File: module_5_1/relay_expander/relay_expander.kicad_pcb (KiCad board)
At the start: 2 copper layers, 1 part, among them U1 STM32G030F6Px

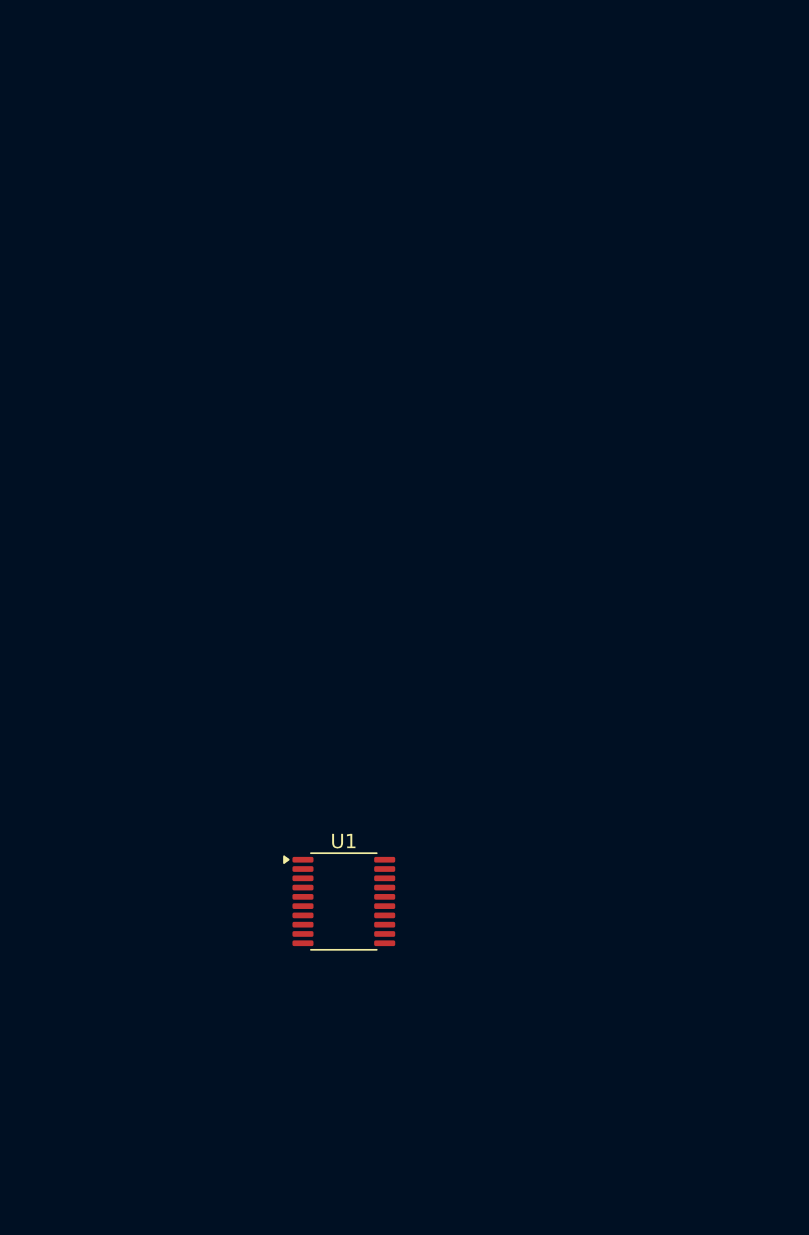
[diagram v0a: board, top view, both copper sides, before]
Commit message: * Schematic almost done * First approximation of PCB is ready, but I would like to move all connectors to one side
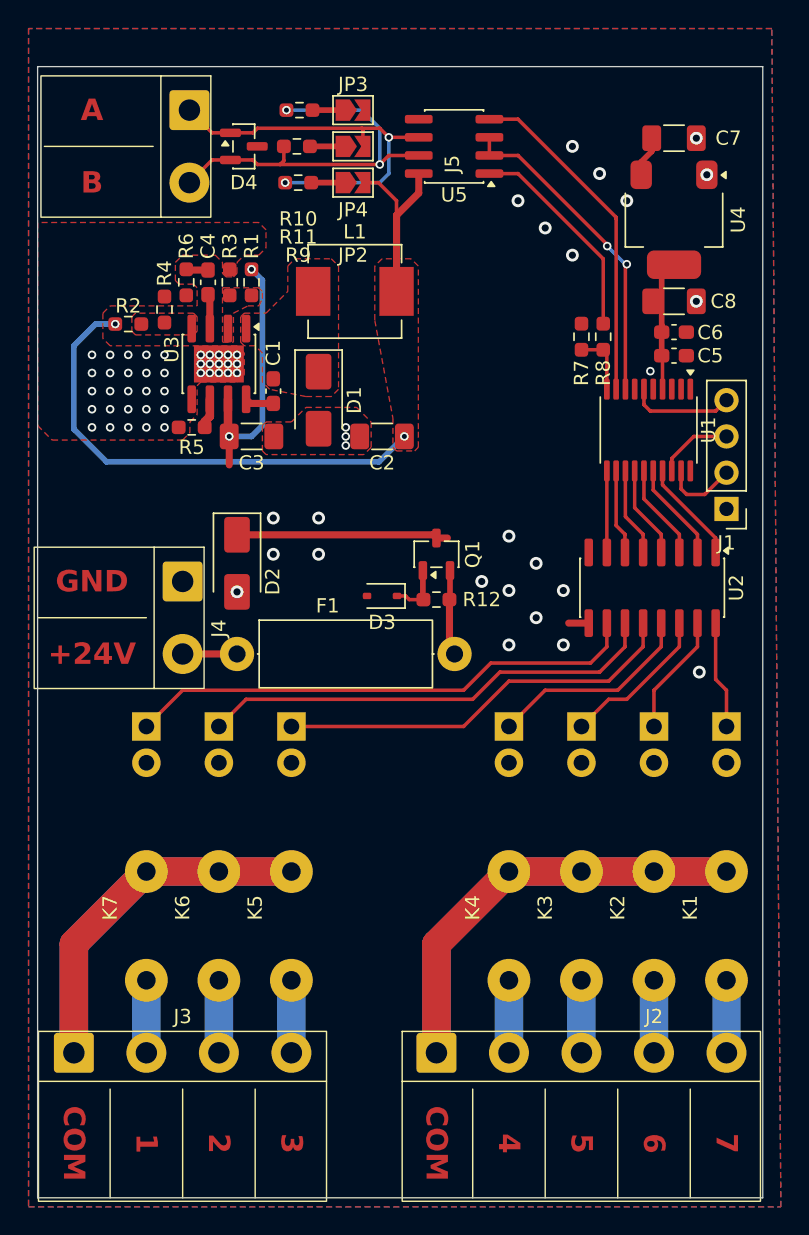
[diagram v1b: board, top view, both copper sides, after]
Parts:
- added C1: 100nF, Capacitor_SMD:C_0603_1608Metric_Pad1.08x0.95mm_HandSolder, F.Cu at (147.1, 45.1)
- added C2: 22uF, Capacitor_SMD:C_1206_3216Metric_Pad1.33x1.80mm_HandSolder, F.Cu at (154.8, 48.3)
- added C3: 10uF, Capacitor_SMD:C_1206_3216Metric_Pad1.33x1.80mm_HandSolder, F.Cu at (145.6, 48.3)
- added C4: 150pF, Capacitor_SMD:C_0603_1608Metric_Pad1.08x0.95mm_HandSolder, F.Cu at (142.6, 37.5)
- added C5: 100nF, Capacitor_SMD:C_0603_1608Metric_Pad1.08x0.95mm_HandSolder, F.Cu at (175.2, 42.7)
- added C6: 4.7uF, Capacitor_SMD:C_0603_1608Metric_Pad1.08x0.95mm_HandSolder, F.Cu at (175.2, 41.0)
- added C7: 10uF, Capacitor_SMD:C_1206_3216Metric_Pad1.33x1.80mm_HandSolder, F.Cu at (175.2, 27.4)
- added C8: 22uF, Capacitor_SMD:C_1206_3216Metric_Pad1.33x1.80mm_HandSolder, F.Cu at (175.2, 38.8)
- added D1: SS34, Diode_SMD:D_SMA, F.Cu at (150.3, 45.8)
- added D2: SMAJ28A, Diode_SMD:D_SMA, F.Cu at (144.6, 57.2)
- added D3: BZX384-B10, Diode_SMD:D_SOD-323, F.Cu at (154.8, 59.5)
- added D4: SM712_SOT23, Package_TO_SOT_SMD:SOT-23, F.Cu at (145.1, 28.0)
- added F1: 1A, Resistor_THT:R_Axial_DIN0414_L11.9mm_D4.5mm_P15.24mm_Horizontal, F.Cu at (144.6, 63.6)
- added J1: PLS-4, Connector_PinHeader_2.54mm:PinHeader_1x04_P2.54mm_Vertical, F.Cu at (178.9, 53.4)
- added J2: 2EDGR-5.08-05P, GMP_library:2EDGR-5.08-05P, F.Cu at (158.6, 91.5)
- added J3: 2EDGR-5.08-04P, GMP_library:2EDGR-5.08-04P, F.Cu at (133.2, 91.5)
- added J4: 2EDGR-5.08-02P, GMP_library:2EDGR-5.08-02P, F.Cu at (140.8, 58.5)
- added J5: 2EDGR-5.08-02P, GMP_library:2EDGR-5.08-02P, F.Cu at (141.3, 25.5)
- added JP2: SP, Jumper:SolderJumper-2_P1.3mm_Open_TrianglePad1.0x1.5mm, F.Cu at (152.7, 30.5)
- added JP3: SP, Jumper:SolderJumper-2_P1.3mm_Open_TrianglePad1.0x1.5mm, F.Cu at (152.7, 25.5)
- added JP4: SP, Jumper:SolderJumper-2_P1.3mm_Open_TrianglePad1.0x1.5mm, F.Cu at (152.7, 28.0)
- added K1: HF49FD/024-1H12, GMP_library:Relay_HF41F_24-HS_Vertical, F.Cu at (178.9, 68.6)
- added K2: HF49FD/024-1H12, GMP_library:Relay_HF41F_24-HS_Vertical, F.Cu at (173.8, 68.6)
- added K3: HF49FD/024-1H12, GMP_library:Relay_HF41F_24-HS_Vertical, F.Cu at (168.7, 68.6)
- added K4: HF49FD/024-1H12, GMP_library:Relay_HF41F_24-HS_Vertical, F.Cu at (163.6, 68.6)
- added K5: HF49FD/024-1H12, GMP_library:Relay_HF41F_24-HS_Vertical, F.Cu at (148.4, 68.6)
- added K6: HF49FD/024-1H12, GMP_library:Relay_HF41F_24-HS_Vertical, F.Cu at (143.3, 68.6)
- added K7: HF49FD/024-1H12, GMP_library:Relay_HF41F_24-HS_Vertical, F.Cu at (138.2, 68.6)
- added L1: 4.7uH, Inductor_SMD:L_Vishay_IHLP-2525, F.Cu at (152.8, 38.2)
- added Q1: AO3401A, Package_TO_SOT_SMD:SOT-23-3, F.Cu at (158.6, 56.6)
- added R1: 100kOhm, Resistor_SMD:R_0603_1608Metric_Pad0.98x0.95mm_HandSolder, F.Cu at (145.6, 37.5)
- added R10: 560, Resistor_SMD:R_0603_1608Metric_Pad0.98x0.95mm_HandSolder, F.Cu at (149.0, 25.5)
- added R11: 120, Resistor_SMD:R_0603_1608Metric_Pad0.98x0.95mm_HandSolder, F.Cu at (148.8, 28.0)
- added R12: 100kOhm, Resistor_SMD:R_0603_1608Metric_Pad0.98x0.95mm_HandSolder, F.Cu at (158.6, 59.7)
- added R2: 210kOhm, Resistor_SMD:R_0603_1608Metric_Pad0.98x0.95mm_HandSolder, F.Cu at (137.0, 40.4)
- added R3: 24.9kOhm, Resistor_SMD:R_0603_1608Metric_Pad0.98x0.95mm_HandSolder, F.Cu at (144.1, 37.5)
- added R4: 40.2kOhm, Resistor_SMD:R_0603_1608Metric_Pad0.98x0.95mm_HandSolder, F.Cu at (139.5, 39.4)
- added R5: 100kOhm, Resistor_SMD:R_0603_1608Metric_Pad0.98x0.95mm_HandSolder, F.Cu at (141.4, 47.7)
- added R6: 100kOhm, Resistor_SMD:R_0603_1608Metric_Pad0.98x0.95mm_HandSolder, F.Cu at (141.0, 37.5)
- added R7: 2k, Resistor_SMD:R_0603_1608Metric_Pad0.98x0.95mm_HandSolder, F.Cu at (168.7, 41.3)
- added R8: 1k, Resistor_SMD:R_0603_1608Metric_Pad0.98x0.95mm_HandSolder, F.Cu at (170.2, 41.3)
- added R9: 560, Resistor_SMD:R_0603_1608Metric_Pad0.98x0.95mm_HandSolder, F.Cu at (148.9, 30.5)
- added U2: ULN2003A, Package_SO:SOIC-16_3.9x9.9mm_P1.27mm, F.Cu at (173.7, 58.9)
- added U3: MP1584, Package_SO:SOIC-8_3.9x4.9mm_P1.27mm, F.Cu at (143.3, 43.2)
- added U4: AMS1117-3.3, Package_TO_SOT_SMD:SOT-223-3_TabPin2, F.Cu at (175.2, 33.1)
- added U5: MAX3078E, Package_SO:SOIC-8_3.9x4.9mm_P1.27mm, F.Cu at (159.8, 28.0)
- moved U1 39.3 mm to (173.4, 47.9), turned to -90 degrees
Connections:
- U1 pad 10: unconnected-(U1-PA3-Pad10) -> /RX
- U1 pad 11: unconnected-(U1-PA4-Pad11) -> Net-(U1-PA4)
- U1 pad 12: unconnected-(U1-PA5-Pad12) -> Net-(U1-PA5)
- U1 pad 13: unconnected-(U1-PA6-Pad13) -> Net-(U1-PA6)
- U1 pad 14: unconnected-(U1-PA7-Pad14) -> Net-(U1-PA7)
- U1 pad 15: unconnected-(U1-PA8/PB0/PB1/PB2-Pad15) -> Net-(U1-PA8/PB0/PB1/PB2)
- U1 pad 16: unconnected-(U1-PA9/PA11-Pad16) -> Net-(U1-PA9/PA11)
- U1 pad 17: unconnected-(U1-PA10/PA12-Pad17) -> Net-(U1-PA10/PA12)
- U1 pad 18: unconnected-(U1-PA13-Pad18) -> /SDIO
- U1 pad 19: unconnected-(U1-PA14/PA15-Pad19) -> /SCLK
- U1 pad 4: unconnected-(U1-VDD-Pad4) -> +3V3
- U1 pad 5: unconnected-(U1-VSS-Pad5) -> GND
- U1 pad 6: unconnected-(U1-NRST-Pad6) -> /NRST
- U1 pad 8: unconnected-(U1-PA1-Pad8) -> /DE
- U1 pad 9: unconnected-(U1-PA2-Pad9) -> /TX
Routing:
- net Net-(J2-Pin_1): track 0.00 -> 60.1 mm
- net Net-(J3-Pin_1): track 0.00 -> 49.9 mm
- net +5V: track 0.00 -> 49.9 mm, vias 0 -> 2
- net Net-(U2-O7): track 0.00 -> 36.2 mm
- net +24V: track 0.00 -> 34.8 mm, vias 0 -> 2
- net Net-(U2-O6): track 0.00 -> 32.4 mm
- net Net-(D4-A1): track 0.00 -> 29.1 mm, vias 0 -> 2
- net Net-(D4-A2): track 0.00 -> 28.7 mm, vias 0 -> 2
- net Net-(U2-O5): track 0.00 -> 28.6 mm
- net /TX: track 0.00 -> 23.8 mm
- net /DE: track 0.00 -> 22.9 mm, vias 0 -> 2
- net Net-(U5-RO): track 0.00 -> 15.0 mm
- net Net-(U2-O4): track 0.00 -> 14.6 mm
- net Net-(U2-O3): track 0.00 -> 10.8 mm
- net +3V3: track 0.00 -> 10.1 mm
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- added copper zone on F.Cu, net +5V
- added copper zone on B.Cu, net GND
- added copper zone on F.Cu, net GND
- added copper zone on F.Cu, net Net-(D4-A1)
- added copper zone on F.Cu, net Net-(U3-En)
- added copper zone on F.Cu, net Net-(U3-FB)
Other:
- board outline added: 50.8 x 79.2 mm
- board text added: "+24V"
- board text added: "1"
- board text added: "2"
- board text added: "3"
- board text added: "4"
- board text added: "5"
- board text added: "6"
- board text added: "7"
- board text added: "A"
- board text added: "B"
- board text added: "COM"
- board text added: "GND"
